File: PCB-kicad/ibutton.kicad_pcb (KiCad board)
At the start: 2 copper layers, 50.8 x 81.3 mm, 30 parts, among them J1 I_BUTTON, J2 IB_READ, J3 BATTERY, J4 USB_OTG, Q1 BC847, Q2 BC847, SW1 SW_Push, U1 ATMEGA8-16AU, U2 CH340G, Y1 12MHz

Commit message: готов прототип печатной платы
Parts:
- removed C2: 0.1mF, Capacitor_SMD:C_0805_2012Metric_Pad1.15x1.40mm_HandSolder
- moved R3 29.4 mm to (27.1, 77.5)
- moved C5 23.8 mm to (78.1, 78.7), turned to 180 degrees
- moved R1 23.4 mm to (29.6, 68.6)
- moved C1 22.5 mm to (71.8, 91.7), turned to 90 degrees
- moved R4 18.4 mm to (76.2, 66.3), turned to 90 degrees
- moved R2 18.2 mm to (56.8, 81.3)
- moved R5 17.7 mm to (75.3, 61.6)
- moved SW1 16.1 mm to (50.2, 48.3)
- moved Q2 13.5 mm to (72.9, 66.9), turned to 270 degrees
- moved J2 12.1 mm to (35.6, 87.0)
- moved J1 10.8 mm to (37.5, 71.1)
- moved R8 10.3 mm to (69.5, 108.6), turned to 180 degrees
- moved Q1 10.2 mm to (37.8, 80.4)
- moved R6 6.21 mm to (61.4, 111.8)
- moved C3 4.29 mm to (78.7, 67.6), turned to 90 degrees
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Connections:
- D2 pad 2: Net-(C2-Pad1) -> Net-(C3-Pad1)
- R4 pad 1: Net-(C2-Pad1) -> Net-(C3-Pad1)
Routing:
- net Net-(C3-Pad1): track 0.00 -> 26.9 mm
- net Net-(U1-Pad31): track 0.00 -> 13.7 mm
- net Net-(U1-Pad30): track 0.00 -> 11.0 mm
- net Net-(D3-Pad1): track 0.00 -> 9.91 mm
- net Net-(Q2-Pad3): track 0.00 -> 5.34 mm
- net Net-(C1-Pad1): track 0.00 -> 3.18 mm
- net Net-(C5-Pad1): track 0.00 -> 2.71 mm
- net Net-(Q2-Pad1): track 0.00 -> 2.37 mm

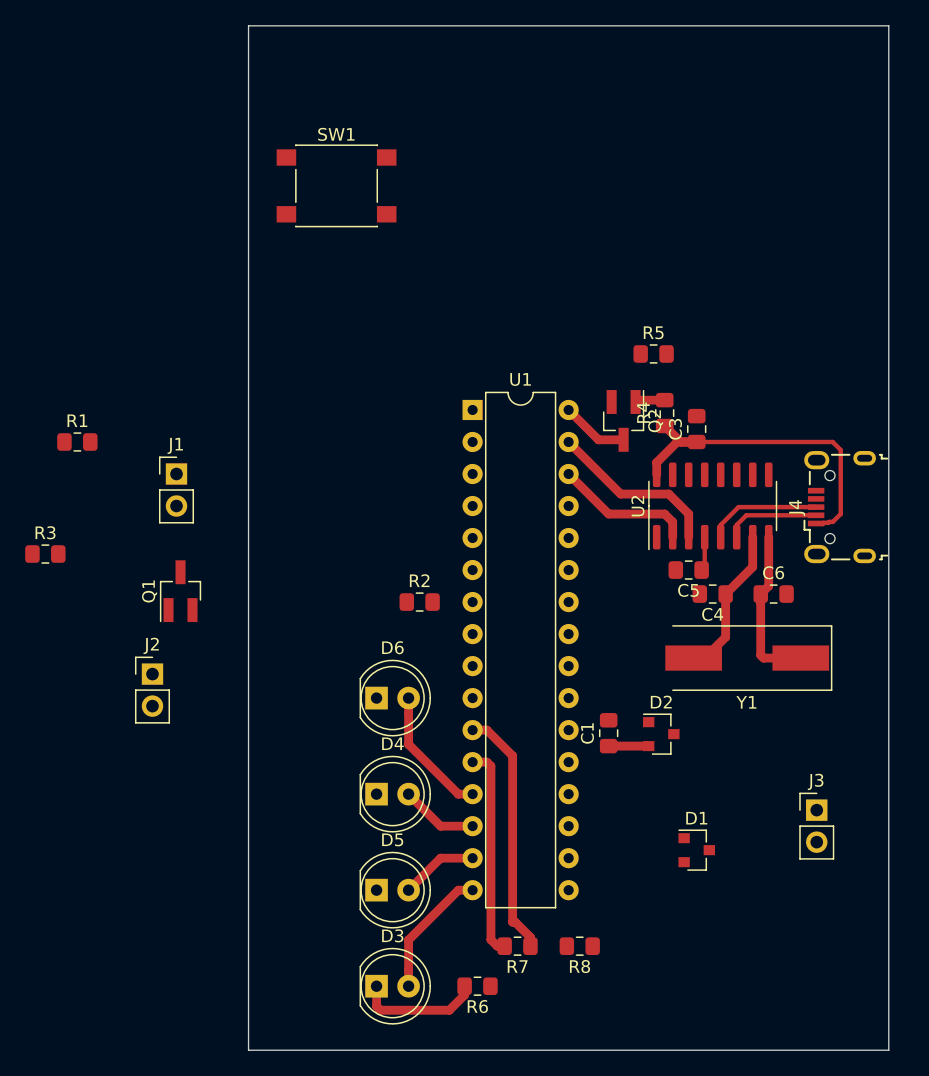
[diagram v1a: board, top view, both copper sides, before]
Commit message: версия печатной платы поменьше
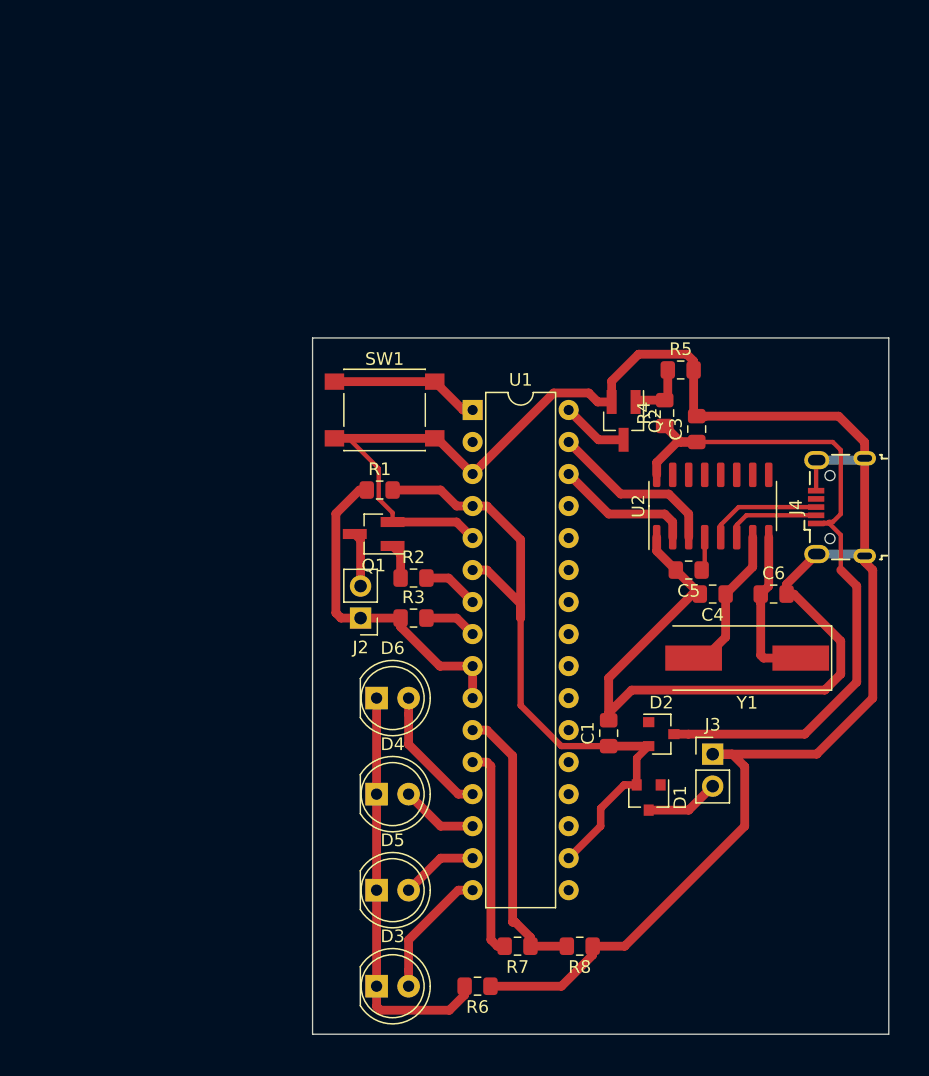
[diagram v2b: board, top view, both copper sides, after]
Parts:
- removed J1: I_BUTTON, Connector_PinHeader_2.54mm:PinHeader_1x02_P2.54mm_Vertical
- moved R3 29.6 mm to (56.3, 82.5)
- moved R1 24.3 mm to (53.6, 72.4)
- moved SW1 18.2 mm to (54.0, 66.0)
- moved J2 17.1 mm to (52.1, 82.5), turned to 180 degrees
- moved Q1 16.0 mm to (53.1, 75.9), turned to 180 degrees
- moved J3 9.38 mm to (80.0, 93.3)
- moved D1 5.65 mm to (74.9, 96.8), turned to 270 degrees
- moved R5 2.50 mm to (77.5, 62.9)
- moved R2 1.97 mm to (56.3, 79.4)
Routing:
- net GND: track 0.00 -> 200.5 mm
- net Net-(C1-Pad1): track 3.18 -> 54.6 mm
- net Net-(C3-Pad1): track 26.9 -> 57.7 mm
- net Net-(J1-Pad1): track 0.00 -> 26.6 mm
- net Net-(D3-Pad1): track 9.91 -> 32.8 mm
- net Net-(SW1-Pad1): track 0.00 -> 11.9 mm
- net Net-(D1-Pad2): track 0.00 -> 5.87 mm
- net Net-(R2-Pad2): track 0.00 -> 4.45 mm
- net Net-(J1-Pad2): track 0.00 -> 4.32 mm
- net Net-(R3-Pad2): track 0.00 -> 4.19 mm
- net Net-(R7-Pad1): track 19.8 -> 22.7 mm
- net Net-(Q1-Pad1): track 0.00 -> 2.81 mm
- net Net-(Q2-Pad1): track 2.37 -> 4.87 mm
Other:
- board size 50.8 x 81.3 mm -> 45.7 x 55.2 mm

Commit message: небольшой фикс
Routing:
- net Net-(C6-Pad1): track 12.9 -> 11.2 mm
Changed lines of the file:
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@@
     (thickness 1.6)
     (drawings 5)
-    (tracks 191)
+    (tracks 189)
     (zones 0)
     (modules 28)
@@
   (segment (start 84.455 80.01) (end 84.455 76.135) (width 0.7) (layer F.Cu) (net 6))
   (segment (start 83.82 80.645) (end 84.455 80.01) (width 0.7) (layer F.Cu) (net 6))
-  (segment (start 83.82 85.5) (end 83.82 81.345) (width 0.7) (layer F.Cu) (net 6))
-  (segment (start 84.045 85.725) (end 83.82 85.5) (width 0.7) (layer F.Cu) (net 6))
-  (segment (start 83.82 81.345) (end 83.82 80.645) (width 0.7) (layer F.Cu) (net 6))
-  (segment (start 86.995 85.725) (end 84.045 85.725) (width 0.7) (layer F.Cu) (net 6))
+  (segment (start 83.82 82.55) (end 83.82 80.645) (width 0.7) (layer F.Cu) (net 6))
+  (segment (start 86.995 85.725) (end 83.82 82.55) (width 0.7) (layer F.Cu) (net 6))
   (segment (start 78.105 97.79) (end 80.01 95.885) (width 0.7) (layer F.Cu) (net 7))
   (segment (start 74.93 97.79) (end 78.105 97.79) (width 0.7) (layer F.Cu) (net 7))

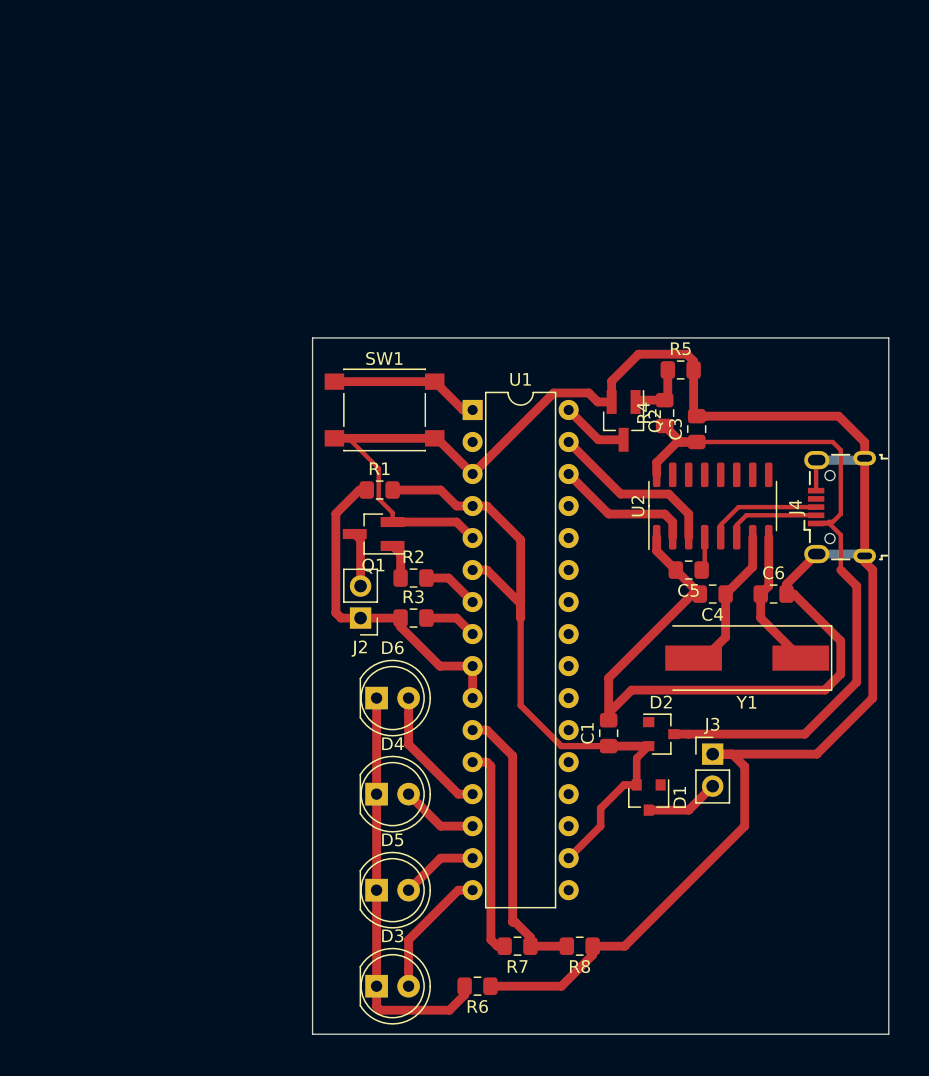
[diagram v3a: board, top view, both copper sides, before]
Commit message: invalid footprint
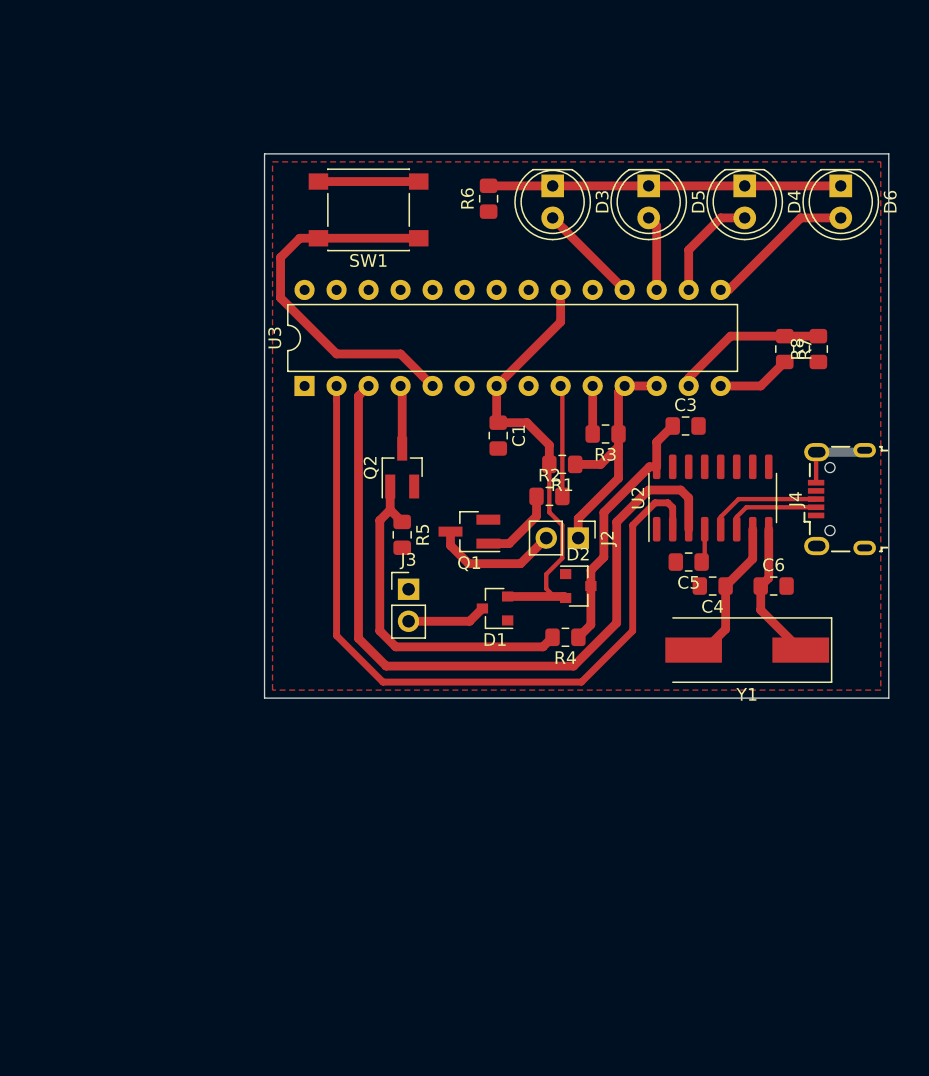
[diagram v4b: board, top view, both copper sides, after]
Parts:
- removed U1: ATMEGA8-16AU, Package_DIP:DIP-32_W7.62mm
- added U3: ATmega8-16PU, Package_DIP:DIP-28_W7.62mm, F.Cu at (47.6, 64.1)
- moved D3 65.0 mm to (67.3, 48.3), turned to 270 degrees
- moved R6 62.5 mm to (62.2, 49.3), turned to 90 degrees
- moved D5 59.9 mm to (74.9, 48.3), turned to 270 degrees
- moved D4 56.4 mm to (82.5, 48.3), turned to 270 degrees
- moved D6 54.8 mm to (90.2, 48.3), turned to 270 degrees
- moved R7 51.9 mm to (85.7, 61.2), turned to 270 degrees
- moved R8 51.0 mm to (88.4, 61.2), turned to 90 degrees
- moved J3 27.4 mm to (55.9, 80.3)
- moved R5 25.7 mm to (55.4, 75.9), turned to 270 degrees
- moved C1 25.2 mm to (63.0, 68.1), turned to 270 degrees
- moved R3 21.1 mm to (71.5, 67.9), turned to 180 degrees
- moved R4 19.5 mm to (68.3, 84.1), turned to 180 degrees
- moved D1 19.3 mm to (62.7, 81.8), turned to 180 degrees
- moved J2 18.4 mm to (69.3, 76.2), turned to 270 degrees
- moved Q2 18.0 mm to (55.4, 70.6), turned to 90 degrees
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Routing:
- net GND: track 200.5 -> 14.3 mm
- net Net-(U2-Pad2): track 11.0 -> 60.7 mm
- net Net-(U2-Pad3): track 13.7 -> 60.7 mm
- net Net-(C3-Pad1): track 57.7 -> 20.2 mm
- net Net-(Q2-Pad1): track 4.87 -> 27.7 mm
- net Net-(C1-Pad1): track 54.6 -> 36.3 mm
- net Net-(SW1-Pad1): track 11.9 -> 29.8 mm
- net Net-(R7-Pad2): track 16.7 -> 5.87 mm
- net Net-(R7-Pad1): track 22.7 -> 12.3 mm
- net Net-(J1-Pad1): track 26.6 -> 20.2 mm
- net Net-(J1-Pad2): track 4.32 -> 10.1 mm
- net Net-(D3-Pad1): track 32.8 -> 27.9 mm
- net Net-(R2-Pad2): track 4.45 -> 8.82 mm
- net Net-(Q1-Pad1): track 2.81 -> 6.29 mm
- net Net-(D4-Pad2): track 6.13 -> 8.67 mm
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- added copper zone on F.Cu, net GND
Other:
- board size 45.7 x 55.2 mm -> 49.5 x 43.2 mm

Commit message: нормальная печатная плата
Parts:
- moved C3 9.92 mm to (87.4, 64.5)
- moved C1 2.03 mm to (63.0, 70.1)
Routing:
- net Net-(C3-Pad1): track 20.2 -> 44.0 mm
- net GND: track 14.3 -> 23.9 mm, vias 0 -> 2
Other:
- board size 49.5 x 43.2 mm -> 49.5 x 43.9 mm
